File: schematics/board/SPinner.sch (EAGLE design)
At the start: 9 parts

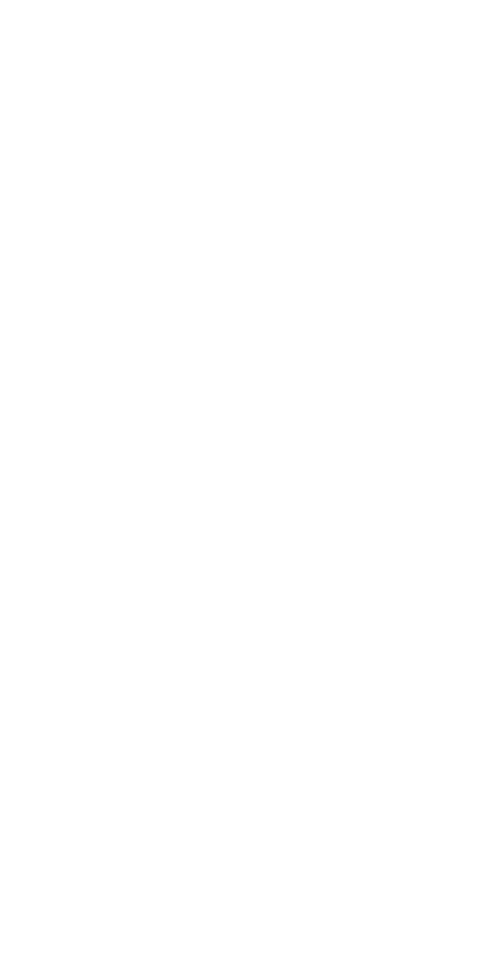
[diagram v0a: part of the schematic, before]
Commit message: Добавлены платы SP
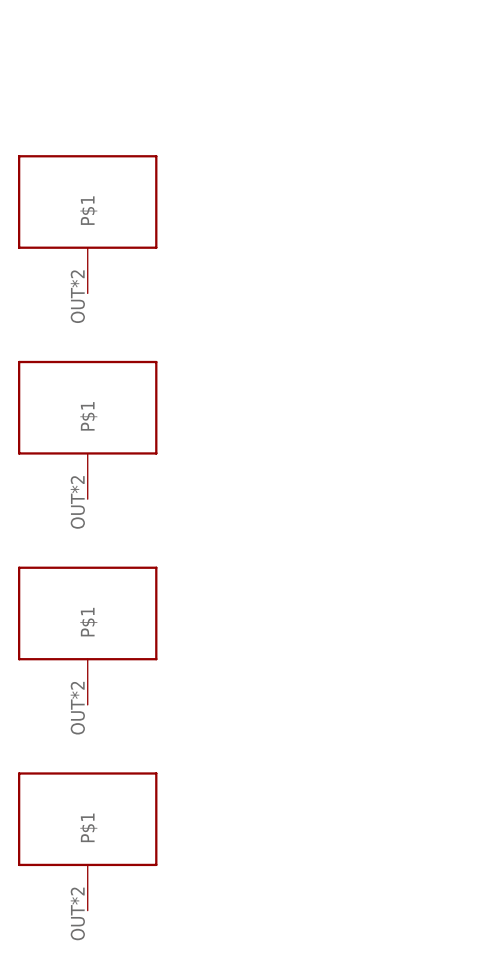
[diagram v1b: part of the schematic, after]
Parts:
- added U$6, U$7, U$8, U$9: GRAFIT-PASSIVE, CanCubeSat:GRAFIT-PASSIVE
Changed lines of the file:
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@@
 <drawing>
 <settings>
-<setting alwaysvectorfont="no"/>
+<setting alwaysvectorfont="yes"/>
 <setting verticaltext="up"/>
 </settings>
@@
 <part name="U$21" library="CanCubeSat" deviceset="KCONNECT" device="" value="KCONNECT"/>
 <part name="U$5" library="CanCubeSat" deviceset="KCONNECT" device="QUAD"/>
+<part name="U$6" library="CanCubeSat" deviceset="GRAFIT-PASSIVE" device=""/>
+<part name="U$7" library="CanCubeSat" deviceset="GRAFIT-PASSIVE" device=""/>
+<part name="U$8" library="CanCubeSat" deviceset="GRAFIT-PASSIVE" device=""/>
+<part name="U$9" library="CanCubeSat" deviceset="GRAFIT-PASSIVE" device=""/>
 </parts>
 <sheets>
@@
 <attribute name="NAME" x="87.122" y="109.982" size="1.27" layer="95"/>
 </instance>
+<instance part="U$6" gate="G$1" x="17.78" y="91.44" smashed="yes"/>
+<instance part="U$7" gate="G$1" x="17.78" y="68.58" smashed="yes"/>
+<instance part="U$8" gate="G$1" x="17.78" y="45.72" smashed="yes"/>
+<instance part="U$9" gate="G$1" x="17.78" y="22.86" smashed="yes"/>
 </instances>
 <busses>

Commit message: Доделаны платы SP
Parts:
- added JP1: 1X02_EMPTY, CanCubeSat:1X02_EMPTY
- added U$10: BUTTON_6X6, CanCubeSat:BUTTON_6X6
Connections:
- new net N$1: JP1.1, U$10.S, U$10.S@1
- new net N$3: JP1.2, U$10.P, U$10.P@1
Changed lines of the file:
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@@
 <part name="U$8" library="CanCubeSat" deviceset="GRAFIT-PASSIVE" device=""/>
 <part name="U$9" library="CanCubeSat" deviceset="GRAFIT-PASSIVE" device=""/>
+<part name="U$10" library="CanCubeSat" deviceset="BUTTON_6X6" device=""/>
+<part name="JP1" library="CanCubeSat" deviceset="1X02_EMPTY" device=""/>
 </parts>
 <sheets>
@@
 <instance part="U$8" gate="G$1" x="17.78" y="45.72" smashed="yes"/>
 <instance part="U$9" gate="G$1" x="17.78" y="22.86" smashed="yes"/>
+<instance part="U$10" gate="G$1" x="-25.4" y="35.56" smashed="yes">
+<attribute name="NAME" x="-32.385" y="33.655" size="1.778" layer="95" rot="R90"/>
+<attribute name="VALUE" x="-29.845" y="38.1" size="1.778" layer="96" rot="R90"/>
+</instance>
+<instance part="JP1" gate="G$1" x="-10.16" y="33.02" smashed="yes">
+<attribute name="NAME" x="-16.51" y="38.735" size="1.778" layer="95"/>
+<attribute name="VALUE" x="-16.51" y="27.94" size="1.778" layer="96"/>
+</instance>
 </instances>
 <busses>
@@
 </segment>
 </net>
+<net name="N$1" class="0">
+<segment>
+<pinref part="U$10" gate="G$1" pin="S@1"/>
+<pinref part="U$10" gate="G$1" pin="S"/>
+<wire x1="-22.86" y1="40.64" x2="-25.4" y2="40.64" width="0.1524" layer="91"/>
+<pinref part="JP1" gate="G$1" pin="1"/>
+<wire x1="-12.7" y1="35.56" x2="-12.7" y2="40.64" width="0.1524" layer="91"/>
+<wire x1="-12.7" y1="40.64" x2="-22.86" y2="40.64" width="0.1524" layer="91"/>
+<junction x="-22.86" y="40.64"/>
+</segment>
+</net>
+<net name="N$3" class="0">
+<segment>
+<pinref part="U$10" gate="G$1" pin="P@1"/>
+<pinref part="U$10" gate="G$1" pin="P"/>
+<wire x1="-22.86" y1="30.48" x2="-25.4" y2="30.48" width="0.1524" layer="91"/>
+<pinref part="JP1" gate="G$1" pin="2"/>
+<wire x1="-12.7" y1="33.02" x2="-12.7" y2="30.48" width="0.1524" layer="91"/>
+<wire x1="-12.7" y1="30.48" x2="-22.86" y2="30.48" width="0.1524" layer="91"/>
+<junction x="-22.86" y="30.48"/>
+</segment>
+</net>

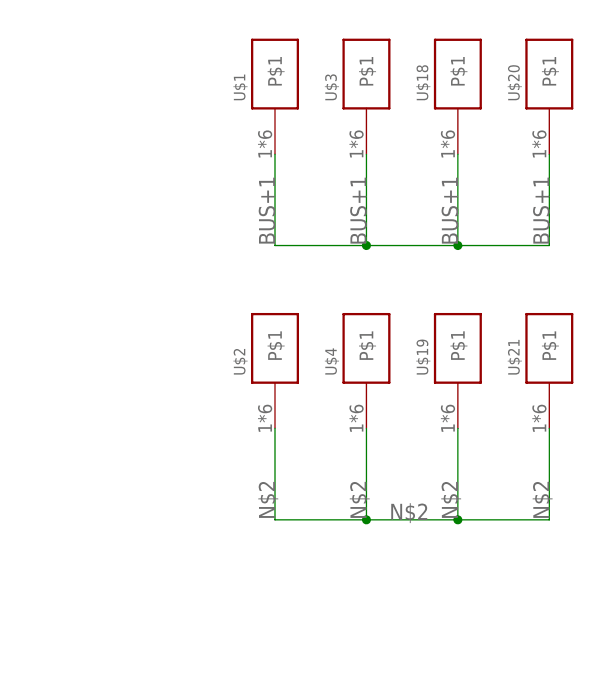
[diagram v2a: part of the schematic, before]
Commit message: Проверил платы SPinner и SPin,внес декоративные правки
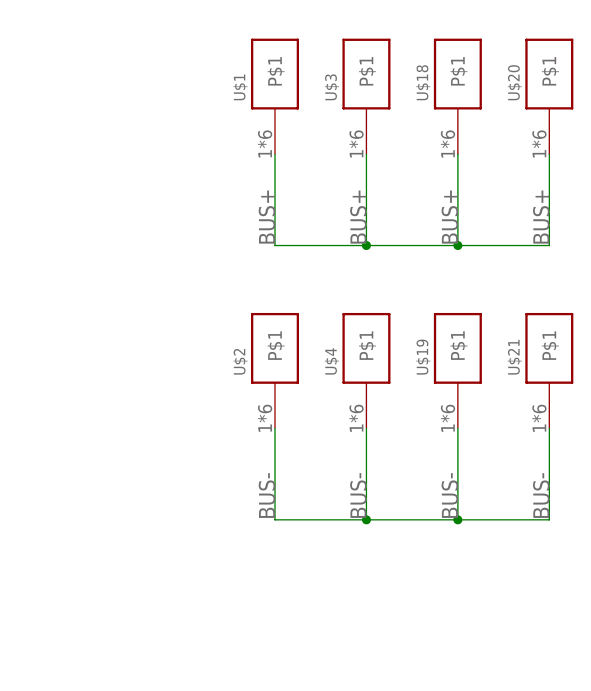
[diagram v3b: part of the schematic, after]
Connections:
- net BUS+1 renamed BUS+
- net N$2 renamed BUS-
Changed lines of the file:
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@@
 </busses>
 <nets>
-<net name="BUS+1" class="0">
+<net name="BUS+" class="0">
 <segment>
 <pinref part="U$1" gate="G$1" pin="P$1"/>
@@
 </segment>
 </net>
-<net name="N$2" class="0">
+<net name="BUS-" class="0">
 <segment>
 <pinref part="U$2" gate="G$1" pin="P$1"/>
@@
 <label x="71.12" y="30.48" size="1.778" layer="95" rot="R90"/>
 <label x="91.44" y="30.48" size="1.778" layer="95" rot="R90"/>
-<label x="83.82" y="30.48" size="1.778" layer="95"/>
 </segment>
 </net>
